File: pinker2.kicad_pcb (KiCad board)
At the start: 2 copper layers, 30 parts, among them J1 XLR3, Q1 BC549C, U1 OPA2134

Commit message: revised to all THT
changed the pot and the Op amp footprints to through hole
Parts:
- R17: footprint Potentiometer_SMD:Potentiometer_Bourns_3214W_Vertical -> Potentiometer_THT:Potentiometer_Bourns_3266X_Horizontal
- U1: footprint Package_SO:SOIC-8-N7_3.9x4.9mm_P1.27mm -> Package_DIP:DIP-8_W7.62mm_Socket
- moved R4 9.17 mm to (143.5, 102.3), turned to 90 degrees
- moved U1 6.59 mm to (146.0, 94.5)
- moved C5 6.04 mm to (152.1, 98.7)
- moved C3 5.01 mm to (161.3, 104.6)
- moved C4 5.01 mm to (161.4, 98.9)
- moved R10 5.01 mm to (165.0, 99.2)
- moved R9 5.01 mm to (165.0, 104.6)
- moved R17 4.16 mm to (132.1, 100.1)
- moved C10 2.62 mm to (136.9, 101.1)
- moved R3 2.08 mm to (140.0, 102.3), turned to 90 degrees
- moved C1 1.47 mm to (149.9, 90.4)
- moved R2 0.52 mm to (133.9, 87.5)
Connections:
- C1 pad 1: Net-(R4-Pad2) -> Net-(C1-Pad1)
- R4 pad 2: Net-(R4-Pad2) -> Net-(C1-Pad1)
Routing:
- net Earth: track 40.2 -> 106.0 mm
- net Net-(C5-Pad2): track 109.5 -> 82.3 mm
- net Net-(C1-Pad1): track 0.00 -> 20.8 mm
- net Net-(R10-Pad2): track 46.0 -> 61.8 mm
- net Net-(R4-Pad2): track 12.4 -> 0.00 mm
- net Net-(C11-Pad1): track 61.5 -> 56.8 mm
- net Net-(R3-Pad2): track 16.2 -> 17.4 mm
- net Net-(C10-Pad2): track 7.88 -> 7.34 mm

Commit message: almost complete
nudged some items, added a ground pour, linked the footprints to a local library (hopefully symbols live there too) added a pdf of the layout to help with visual diffs
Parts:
- C1, C10, C9: footprint Capacitor_THT:CP_Radial_D4.0mm_P1.50mm -> Library:CP_Radial_D4.0mm_P1.50mm
- C11, C5, C6, C8: footprint Capacitor_THT:CP_Radial_D10.0mm_P5.00mm -> Library:CP_Radial_D10.0mm_P5.00mm
- C2, C3, C4, C7: footprint Capacitor_THT:C_Disc_D3.0mm_W1.6mm_P2.50mm -> Library:C_Disc_D3.0mm_W1.6mm_P2.50mm
- J1: footprint Connector_Audio:Jack_XLR_Neutrik_NC3MBH_Horizontal -> Library:Jack_XLR_Neutrik_NC3MBH_Horizontal
- Q1: footprint Package_TO_SOT_THT:TO-92_Inline -> Library:TO-92_Inline
- R1, R10, R11, R12, R13, R14, R15, R2, R3, R4, R5, R6, R7, R8, R9: footprint Resistor_THT:R_Axial_DIN0204_L3.6mm_D1.6mm_P1.90mm_Vertical -> Library:R_Axial_DIN0204_L3.6mm_D1.6mm_P1.90mm_Vertical
- R17: footprint Potentiometer_THT:Potentiometer_Bourns_3266X_Horizontal -> Library:Potentiometer_Bourns_3266X_Horizontal
- U1: footprint Package_DIP:DIP-8_W7.62mm_Socket -> Library:DIP-8_W7.62mm_Socket
- moved R12 16.2 mm to (174.0, 96.0)
- moved R17 2.94 mm to (133.3, 102.7)
- moved R4 2.94 mm to (144.8, 104.9)
- moved C10 2.94 mm to (138.2, 103.7)
- moved R3 2.94 mm to (141.2, 104.9)
- moved C9 2.68 mm to (133.2, 95.9)
- moved Q1 2.68 mm to (127.0, 96.1)
- moved U1 1.80 mm to (146.3, 96.3)
- moved R2 1.80 mm to (134.1, 89.3)
- moved R1 1.67 mm to (128.3, 89.3)
- moved R13 0.76 mm to (189.0, 92.6)
- moved C7 0.65 mm to (189.0, 95.2)
- moved C6 0.57 mm to (183.2, 90.2)
- moved R14 0.40 mm to (189.0, 102.3)
- moved R15 0.25 mm to (189.9, 106.2)
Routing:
- net Earth: track 106.0 -> 18.3 mm
- net Net-(R10-Pad2): track 61.8 -> 45.5 mm
- net Net-(C6-Pad2): track 12.9 -> 6.81 mm
- net Net-(C5-Pad2): track 82.3 -> 87.7 mm
- net Net-(C1-Pad1): track 20.8 -> 24.3 mm
- net Net-(C11-Pad1): track 56.8 -> 59.2 mm
- net Net-(R3-Pad2): track 17.4 -> 18.7 mm
- net Net-(C9-Pad1): track 10.1 -> 11.2 mm
- net Net-(C9-Pad2): track 10.8 -> 11.7 mm
- net Net-(C6-Pad1): track 12.3 -> 11.7 mm
- added copper zone on B.Cu, net Earth
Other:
- board outline added: 71.4 x 24.9 mm

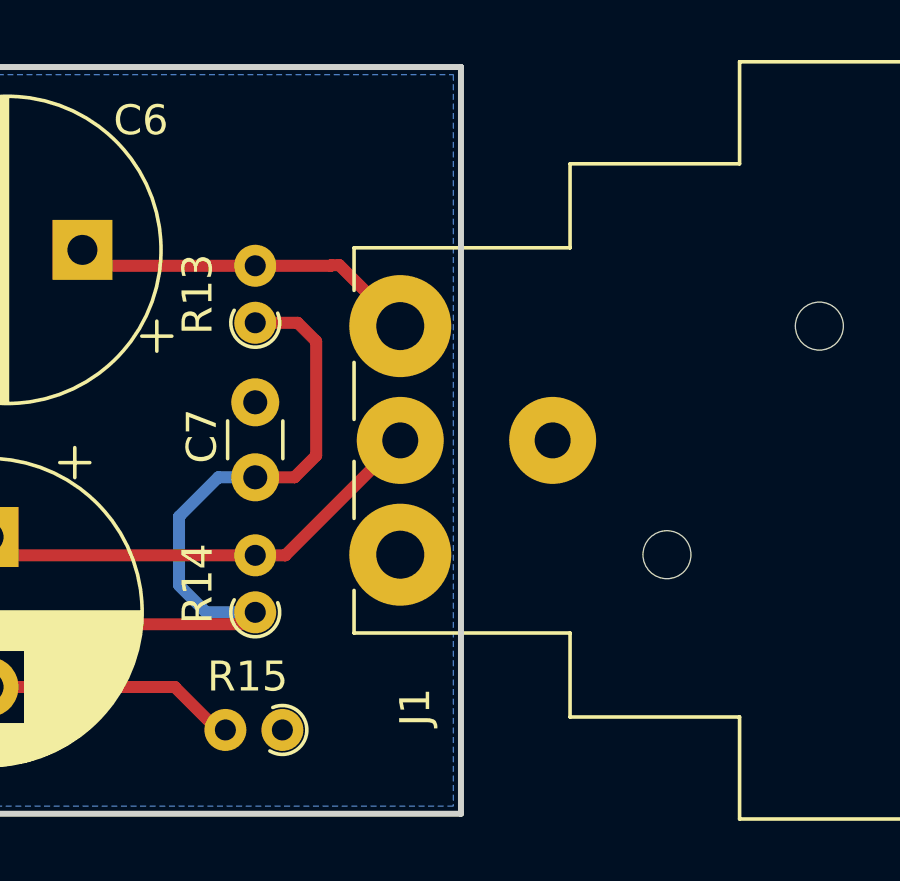
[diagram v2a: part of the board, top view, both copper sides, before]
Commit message: mostly complete
added some silkscreen notes, and deleted some junk files
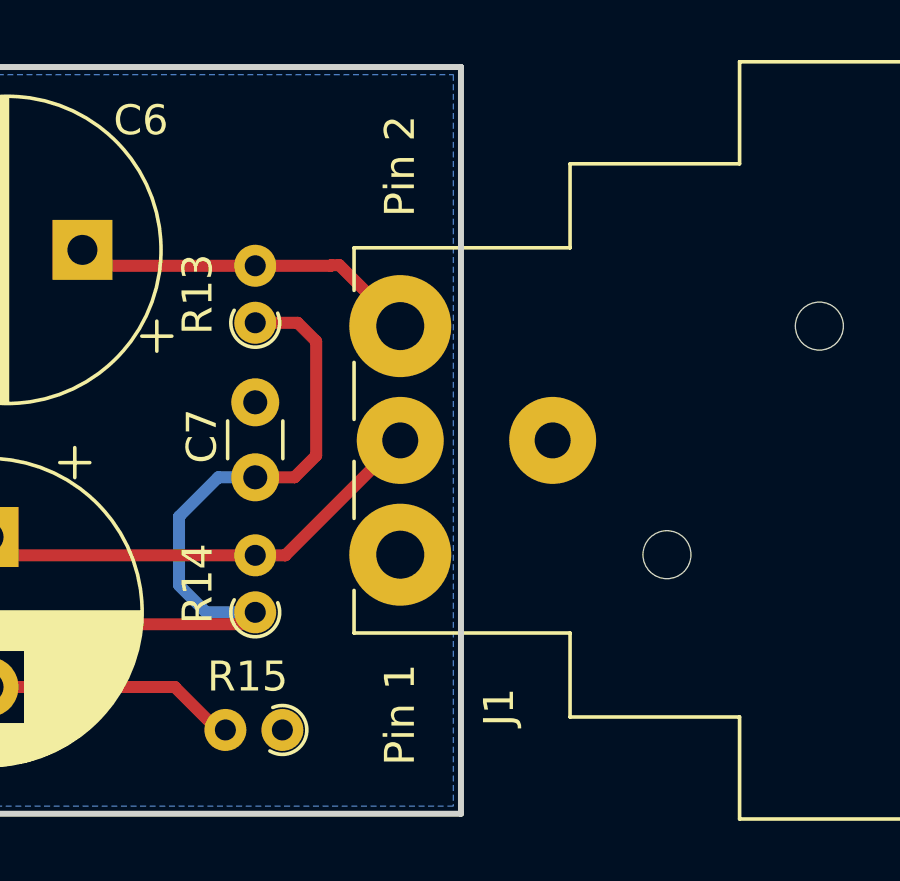
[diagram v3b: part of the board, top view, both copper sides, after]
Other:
- board text added: "+48V Pink noise source Chris Williams 2023"
- board text added: "Pin 1"
- board text added: "Pin 2"
- board text added: "github:chrisfromthepast/pinker2"
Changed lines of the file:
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@@
       (sketchpadsonfab false)
       (subtractmaskfromsilk false)
-      (outputformat 4)
+      (outputformat 1)
       (mirror false)
       (drillshape 0)
@@
     (property "Sheetname" "")
     (attr through_hole)
-    (fp_text reference "J1" (at -5.08 0.5 90) (layer "F.SilkS")
+    (fp_text reference "J1" (at -5.08 3.294 90) (layer "F.SilkS")
       (effects (font (size 1 1) (thickness 0.15)))
     )
@@
   )
   (gr_rect (start 124.46 84.074) (end 195.834 108.966) (layer "Edge.Cuts") (width 0.2) (fill none))
+  (gr_text "+48V Pink noise source\nChris Williams 2023" (at 183.134 86.614) (layer "B.SilkS")
+    (effects (font (size 1.5 1.3) (thickness 0.25)) (justify mirror))
+  )
+  (gr_text "github:chrisfromthepast/pinker2" (at 143.256 107.188) (layer "B.SilkS")
+    (effects (font (size 1.5 1.5) (thickness 0.3)) (justify mirror))
+  )
+  (gr_text "Pin 2" (at 193.802 87.376 90) (layer "F.SilkS")
+    (effects (font (size 1 1) (thickness 0.15)))
+  )
+  (gr_text "Pin 1" (at 193.802 105.664 90) (layer "F.SilkS")
+    (effects (font (size 1 1) (thickness 0.15)))
+  )
   (segment (start 151.399401 90.219) (end 151.399401 90.424) (width 0.4) (layer "F.Cu") (net 1))
   (segment (start 154.242401 87.376) (end 151.399401 90.219) (width 0.4) (layer "F.Cu") (net 1))
